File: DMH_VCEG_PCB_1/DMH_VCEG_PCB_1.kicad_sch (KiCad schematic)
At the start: 0 parts

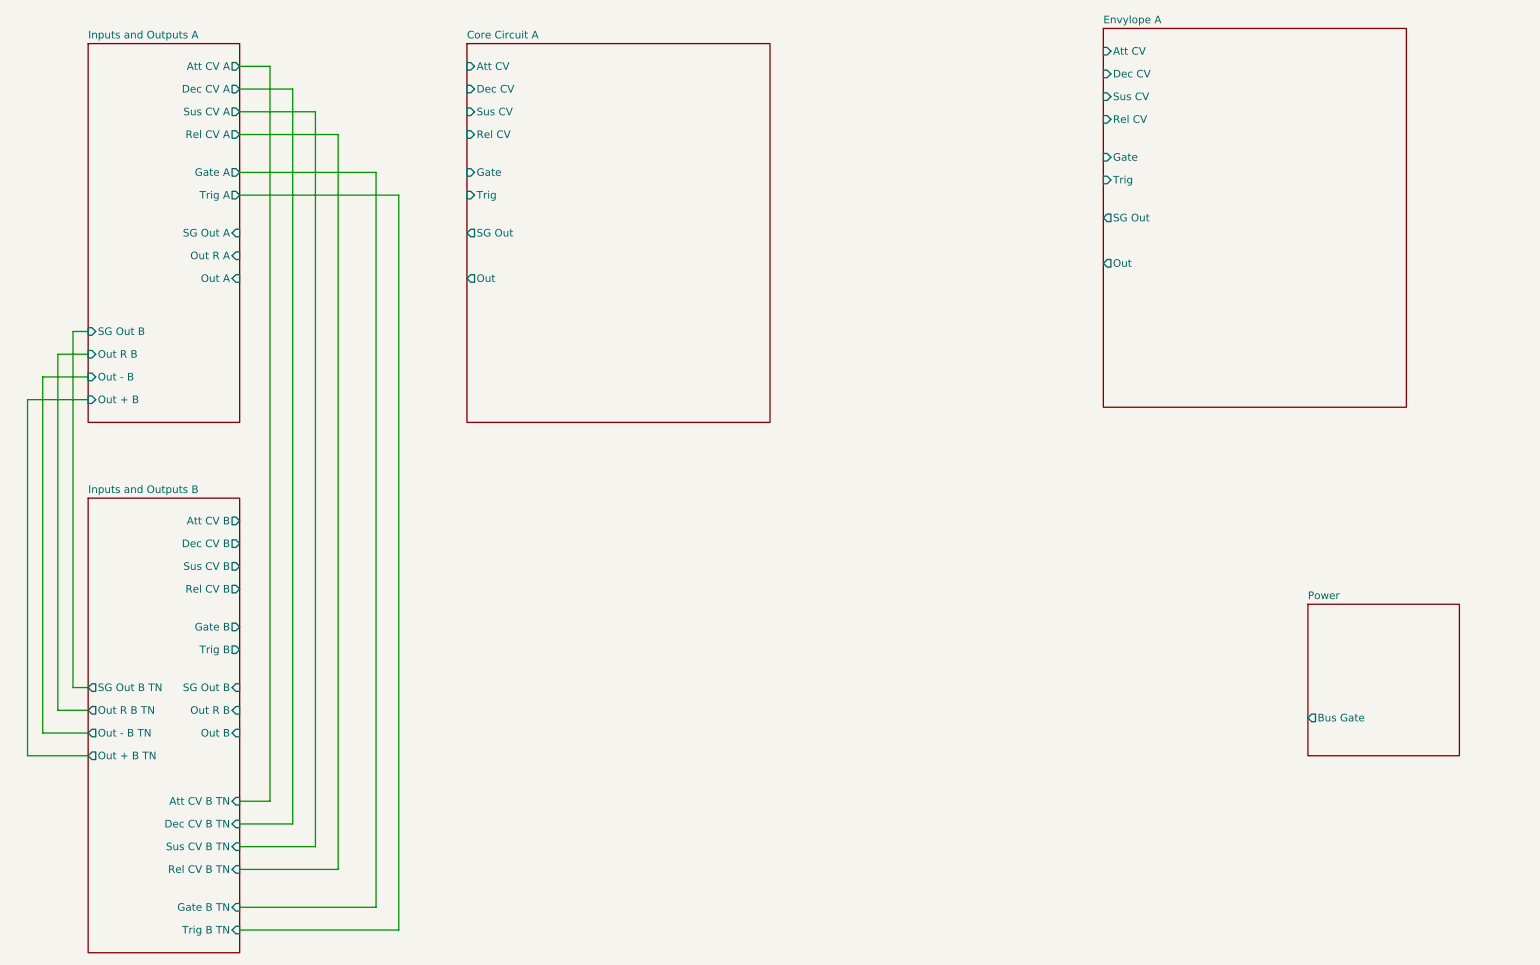
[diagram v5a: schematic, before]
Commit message: Implemented SG Out A
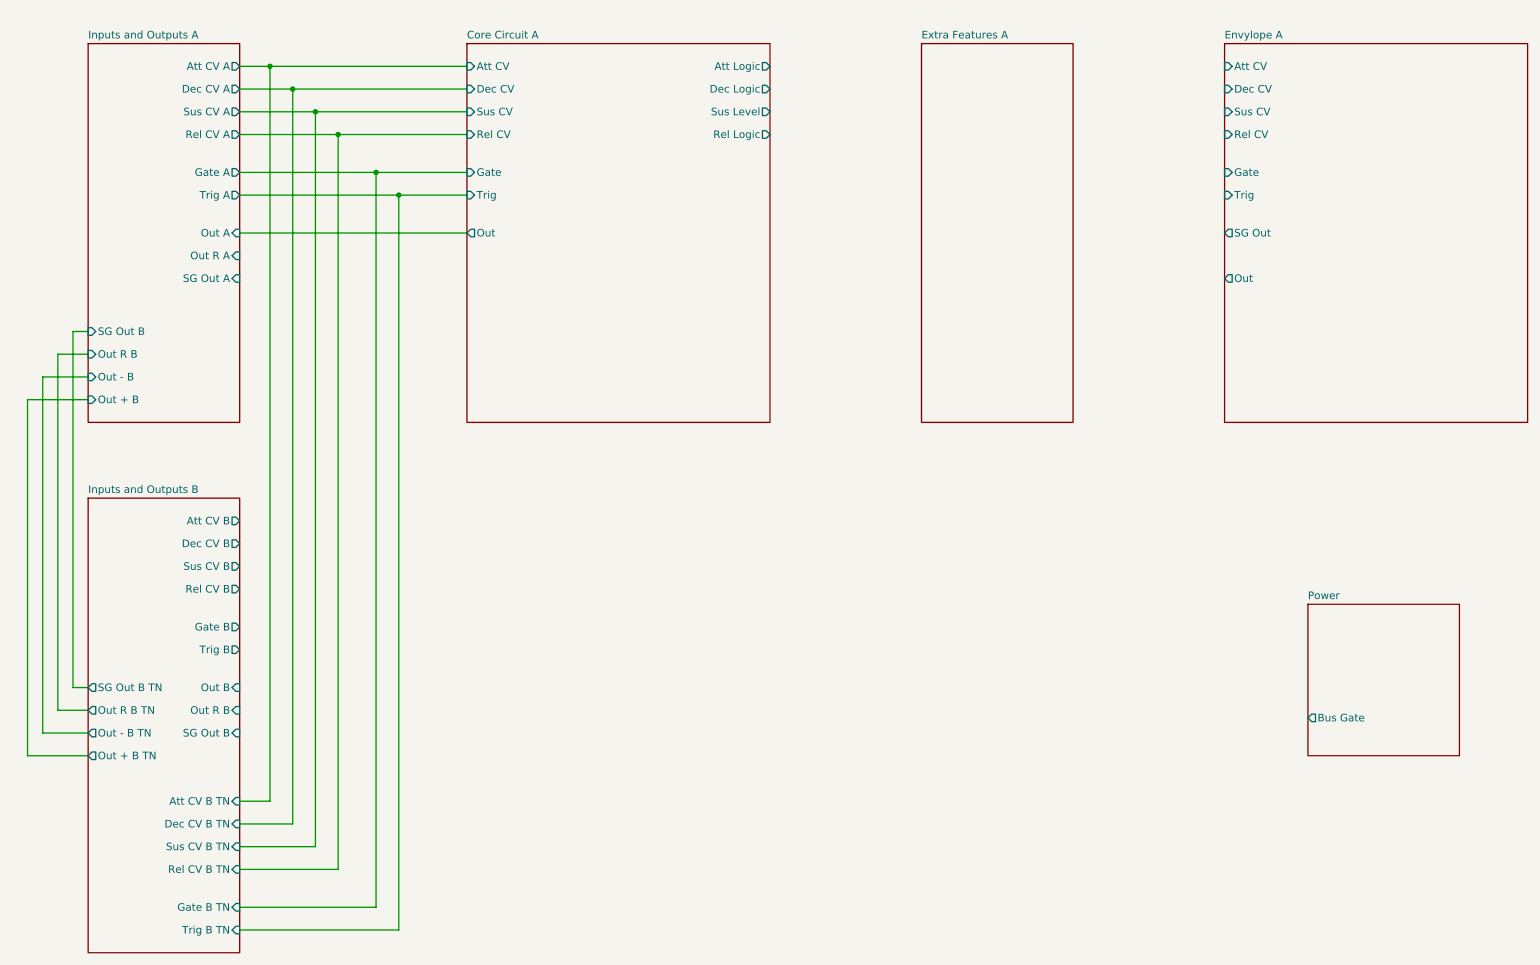
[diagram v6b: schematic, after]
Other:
- added sheet Extra Features A (Extra_Features_A.kicad_sch)
- sheet Core Circuit A ports: added Att Logic, Dec Logic, Rel Logic, Sus Level; removed SG Out
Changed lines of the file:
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@@
 		(comment 1 "PCB for 15cm Kosmo format synthesizer module")
 	)
+	(junction
+		(at 68.58 41.91)
+		(diameter 0)
+		(color 0 0 0 0)
+	)
+	(junction
+		(at 76.2 49.53)
+		(diameter 0)
+		(color 0 0 0 0)
+	)
+	(junction
+		(at 80.01 53.34)
+		(diameter 0)
+		(color 0 0 0 0)
+	)
+	(junction
+		(at 72.39 45.72)
+		(diameter 0)
+		(color 0 0 0 0)
+	)
+	(junction
+		(at 86.36 59.69)
+		(diameter 0)
+		(color 0 0 0 0)
+	)
+	(junction
+		(at 90.17 63.5)
+		(diameter 0)
+		(color 0 0 0 0)
+	)
 	(wire
 		(pts
@@
 	(wire
 		(pts
+			(xy 63.5 69.85) (xy 101.6 69.85)
+		)
+		(stroke
+			(width 0)
+			(type default)
+		)
+	)
+	(wire
+		(pts
 			(xy 63.5 172.72) (xy 76.2 172.72)
 		)
@@
 	(wire
 		(pts
+			(xy 86.36 59.69) (xy 101.6 59.69)
+		)
+		(stroke
+			(width 0)
+			(type default)
+		)
+	)
+	(wire
+		(pts
+			(xy 80.01 53.34) (xy 101.6 53.34)
+		)
+		(stroke
+			(width 0)
+			(type default)
+		)
+	)
+	(wire
+		(pts
 			(xy 63.5 186.69) (xy 90.17 186.69)
 		)
@@
 	(wire
 		(pts
+			(xy 76.2 49.53) (xy 101.6 49.53)
+		)
+		(stroke
+			(width 0)
+			(type default)
+		)
+	)
+	(wire
+		(pts
 			(xy 63.5 165.1) (xy 68.58 165.1)
 		)
@@
 	(wire
 		(pts
+			(xy 72.39 45.72) (xy 101.6 45.72)
+		)
+		(stroke
+			(width 0)
+			(type default)
+		)
+	)
+	(wire
+		(pts
 			(xy 63.5 168.91) (xy 72.39 168.91)
 		)
@@
 		(pts
 			(xy 30.48 153.67) (xy 30.48 93.98)
+		)
+		(stroke
+			(width 0)
+			(type default)
+		)
+	)
+	(wire
+		(pts
+			(xy 90.17 63.5) (xy 101.6 63.5)
+		)
+		(stroke
+			(width 0)
+			(type default)
+		)
+	)
+	(wire
+		(pts
+			(xy 68.58 41.91) (xy 101.6 41.91)
 		)
 		(stroke
@@
 		)
 		(pin "Out B" input
-			(at 63.5 153.67 0)
+			(at 63.5 146.05 0)
 			(effects
 				(font
@@
 		)
 		(pin "SG Out B" input
-			(at 63.5 146.05 0)
+			(at 63.5 153.67 0)
 			(effects
 				(font
@@
 	)
 	(sheet
-		(at 208.28 35.56)
+		(at 228.6 38.1)
 		(size 50.8 63.5)
 		(exclude_from_sim no)
@@
 		)
 		(property "Sheetname" "Envylope A"
-			(at 208.28 34.8484 0)
+			(at 228.6 37.3884 0)
 			(effects
 				(font
@@
 		)
 		(property "Sheetfile" "Envylope_A.kicad_sch"
-			(at 208.28 99.6446 0)
+			(at 228.6 102.1846 0)
 			(effects
 				(font
@@
 		)
 		(pin "Att CV" input
-			(at 208.28 39.37 180)
+			(at 228.6 41.91 180)
 			(effects
 				(font
@@
 		)
 		(pin "Dec CV" input
-			(at 208.28 43.18 180)
+			(at 228.6 45.72 180)
 			(effects
 				(font
@@
 		)
 		(pin "Gate" input
-			(at 208.28 57.15 180)
+			(at 228.6 59.69 180)
 			(effects
 				(font
@@
 		)
 		(pin "Rel CV" input
-			(at 208.28 50.8 180)
+			(at 228.6 53.34 180)
 			(effects
 				(font
@@
 		)
 		(pin "SG Out" output
-			(at 208.28 67.31 180)
+			(at 228.6 69.85 180)
 			(effects
 				(font
@@
 		)
 		(pin "Sus CV" input
-			(at 208.28 46.99 180)
+			(at 228.6 49.53 180)
 			(effects
 				(font
@@
 		)
 		(pin "Trig" input
-			(at 208.28 60.96 180)
+			(at 228.6 63.5 180)
 			(effects
 				(font
@@
 		)
 		(pin "Out" output
-			(at 208.28 74.93 180)
+			(at 228.6 77.47 180)
 			(effects
 				(font
@@
 			)
 		)
-		(pin "SG Out" output
-			(at 101.6 69.85 180)
-			(effects
-				(font
-					(size 1.27 1.27)
-				)
-				(justify left)
-			)
-		)
 		(pin "Sus CV" input
 			(at 101.6 49.53 180)
@@
 		)
 		(pin "Out" output
-			(at 101.6 77.47 180)
-			(effects
-				(font
-					(size 1.27 1.27)
-				)
-				(justify left)
+			(at 101.6 69.85 180)
+			(effects
+				(font
+					(size 1.27 1.27)
+				)
+				(justify left)
+			)
+		)
+		(pin "Att Logic" output
+			(at 152.4 41.91 0)
+			(effects
+				(font
+					(size 1.27 1.27)
+				)
+				(justify right)
+			)
+		)
+		(pin "Dec Logic" output
+			(at 152.4 45.72 0)
+			(effects
+				(font
+					(size 1.27 1.27)
+				)
+				(justify right)
+			)
+		)
+		(pin "Rel Logic" output
+			(at 152.4 53.34 0)
+			(effects
+				(font
+					(size 1.27 1.27)
+				)
+				(justify right)
+			)
+		)
+		(pin "Sus Level" output
+			(at 152.4 49.53 0)
+			(effects
+				(font
+					(size 1.27 1.27)
+				)
+				(justify right)
 			)
 		)
@@
 		)
 		(pin "Out A" input
-			(at 63.5 77.47 0)
+			(at 63.5 69.85 0)
 			(effects
 				(font
@@
 		)
 		(pin "SG Out A" input
-			(at 63.5 69.85 0)
+			(at 63.5 77.47 0)
 			(effects
 				(font
@@
 				)
 			)
+		)
+	)
+	(sheet
+		(at 177.8 38.1)
+		(size 25.4 63.5)
+		(exclude_from_sim no)
+		(in_bom yes)
+		(on_board yes)
+		(dnp no)
+		(fields_autoplaced yes)
+		(stroke
+			(width 0.1524)
+			(type solid)
+		)
+		(fill
+			(color 0 0 0 0.0000)
+		)
+		(property "Sheetname" "Extra Features A"
+			(at 177.8 37.3884 0)
+			(effects
+				(font
+					(size 1.27 1.27)
+				)
+				(justify left bottom)
+			)
+		)
+		(property "Sheetfile" "Extra_Features_A.kicad_sch"
+			(at 177.8 102.1846 0)
+			(effects
+				(font
+					(size 1.27 1.27)
+				)
+				(justify left top)
+				(hide yes)
+			)
+		)
+		(instances
+			(project "DMH_VCEG_PCB_1"
+				(path "/58f4306d-5387-4983-bb08-41a2313fd315"
+					(page "7")
+				)
+			)

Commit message: Added Out R
Ready for breadboarding
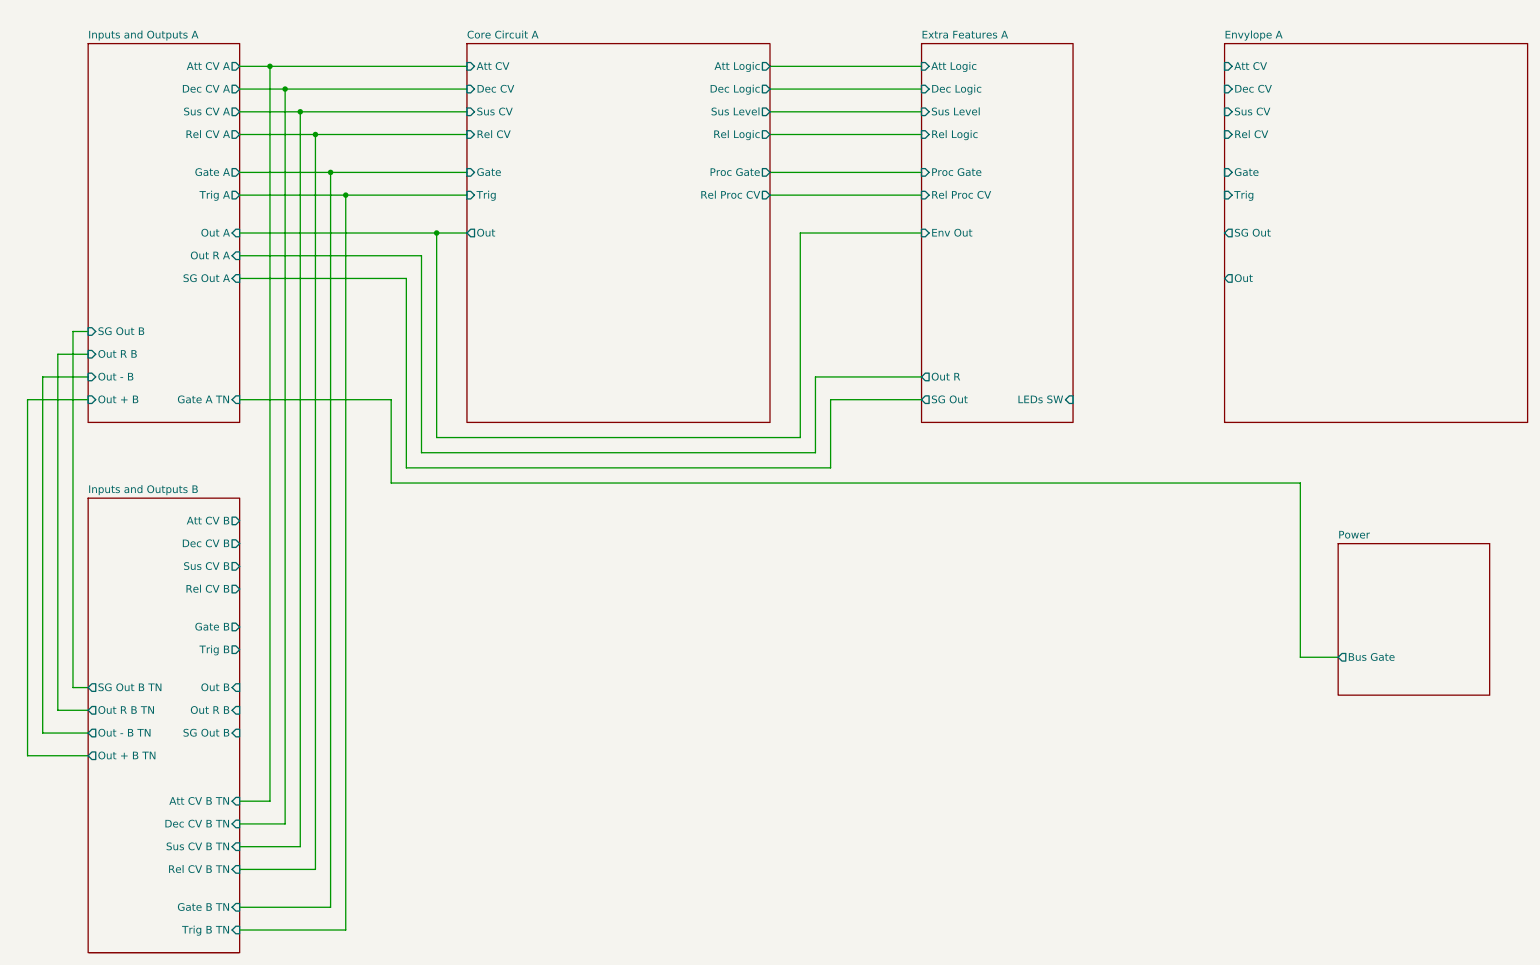
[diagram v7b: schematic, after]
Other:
- sheet Core Circuit A ports: added Proc Gate, Rel Proc CV; removed none
- sheet Extra Features A ports: added Att Logic, Dec Logic, Env Out, LEDs SW, Out R, Proc Gate, Rel Logic, Rel Proc CV, SG Out, Sus Level; removed none
- sheet Inputs and Outputs A ports: added Gate A TN; removed none

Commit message: Corrected Out R design
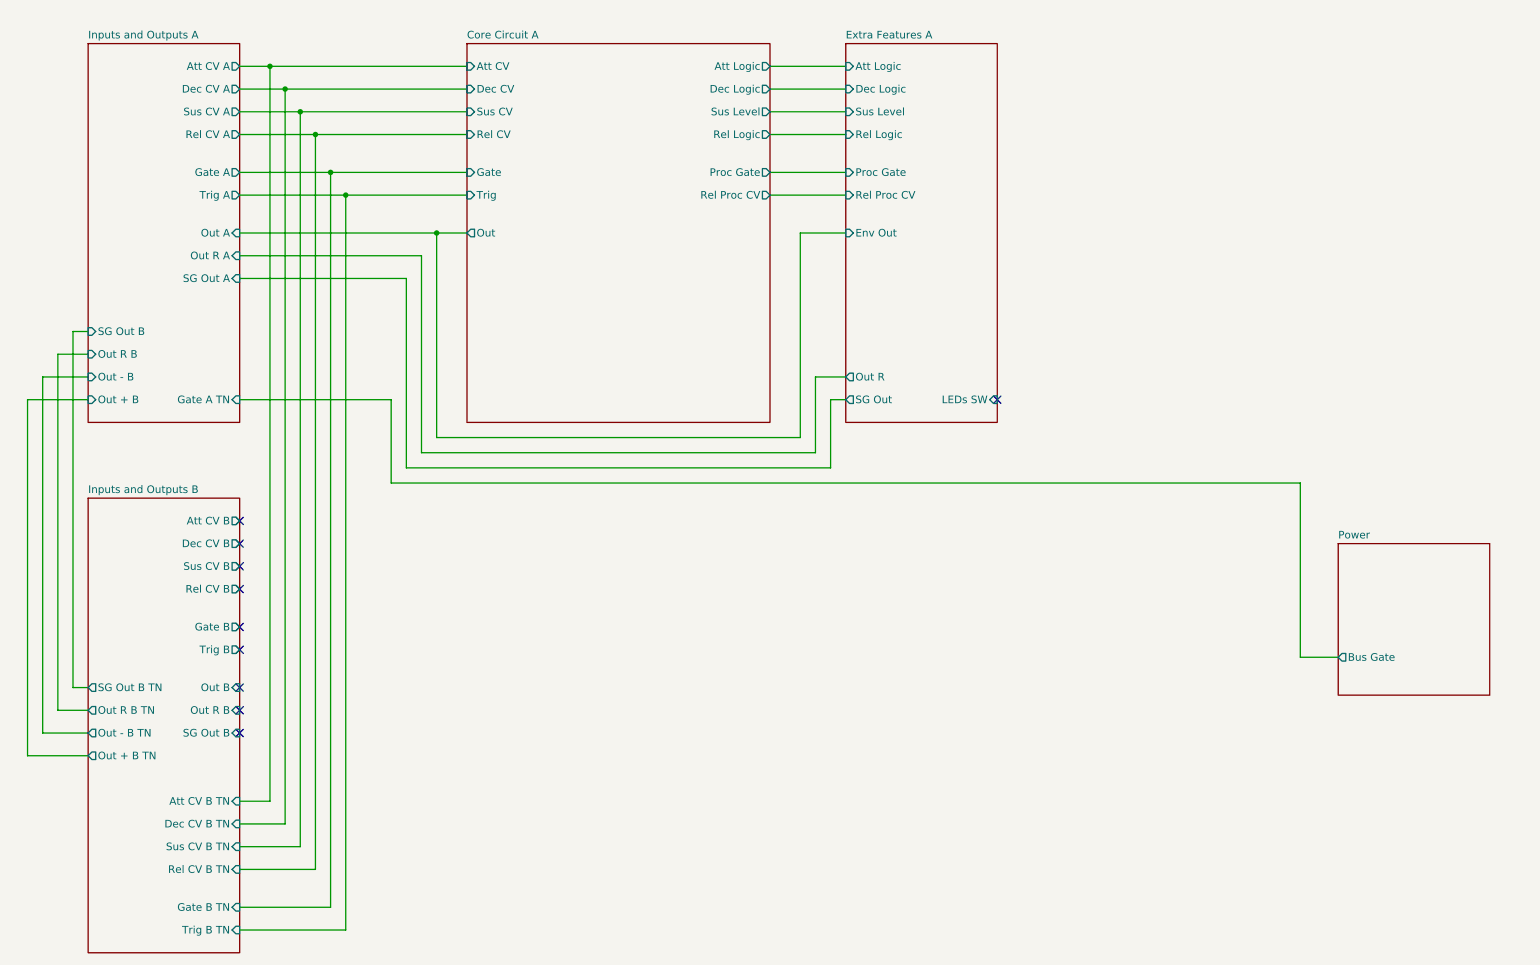
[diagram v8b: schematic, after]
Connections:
- no-connect marks 0 -> 10
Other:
- removed sheet Envylope A
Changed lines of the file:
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@@
 		(color 0 0 0 0)
 	)
-	(wire
-		(pts
-			(xy 152.4 41.91) (xy 177.8 41.91)
+	(no_connect
+		(at 190.5 97.79)
+	)
+	(no_connect
+		(at 63.5 146.05)
+	)
+	(no_connect
+		(at 63.5 149.86)
+	)
+	(no_connect
+		(at 63.5 125.73)
+	)
+	(no_connect
+		(at 63.5 118.11)
+	)
+	(no_connect
+		(at 63.5 121.92)
+	)
+	(no_connect
+		(at 63.5 139.7)
+	)
+	(no_connect
+		(at 63.5 153.67)
+	)
+	(no_connect
+		(at 63.5 135.89)
+	)
+	(no_connect
+		(at 63.5 129.54)
+	)
+	(wire
+		(pts
+			(xy 152.4 41.91) (xy 165.1 41.91)
 		)
 		(stroke
@@
 	(wire
 		(pts
-			(xy 177.8 93.98) (xy 160.02 93.98)
+			(xy 165.1 93.98) (xy 160.02 93.98)
 		)
 		(stroke
@@
 	(wire
 		(pts
-			(xy 157.48 69.85) (xy 177.8 69.85)
+			(xy 157.48 69.85) (xy 165.1 69.85)
 		)
 		(stroke
@@
 	(wire
 		(pts
-			(xy 152.4 45.72) (xy 177.8 45.72)
+			(xy 152.4 45.72) (xy 165.1 45.72)
 		)
 		(stroke
@@
 	(wire
 		(pts
-			(xy 152.4 63.5) (xy 177.8 63.5)
+			(xy 152.4 63.5) (xy 165.1 63.5)
 		)
 		(stroke
@@
 	(wire
 		(pts
-			(xy 152.4 49.53) (xy 177.8 49.53)
-		)
-		(stroke
-			(width 0)
-			(type default)
-		)
-	)
-	(wire
-		(pts
-			(xy 152.4 53.34) (xy 177.8 53.34)
+			(xy 152.4 49.53) (xy 165.1 49.53)
+		)
+		(stroke
+			(width 0)
+			(type default)
+		)
+	)
+	(wire
+		(pts
+			(xy 152.4 53.34) (xy 165.1 53.34)
 		)
 		(stroke
@@
 	(wire
 		(pts
-			(xy 152.4 59.69) (xy 177.8 59.69)
+			(xy 152.4 59.69) (xy 165.1 59.69)
 		)
 		(stroke
@@
 	(wire
 		(pts
-			(xy 162.56 97.79) (xy 177.8 97.79)
+			(xy 162.56 97.79) (xy 165.1 97.79)
 		)
 		(stroke
@@
 			(project "DMH_VCEG_PCB_1"
 				(path "/58f4306d-5387-4983-bb08-41a2313fd315"
-					(page "4")
+					(page "10")
 				)
 			)
@@
 	)
 	(sheet
-		(at 228.6 38.1)
-		(size 50.8 63.5)
-		(exclude_from_sim no)
-		(in_bom yes)
-		(on_board yes)
-		(dnp no)
-		(fields_autoplaced yes)
-		(stroke
-			(width 0.1524)
-			(type solid)
-		)
-		(fill
-			(color 0 0 0 0.0000)
-		)
-		(property "Sheetname" "Envylope A"
-			(at 228.6 37.3884 0)
-			(effects
-				(font
-					(size 1.27 1.27)
-				)
-				(justify left bottom)
-			)
-		)
-		(property "Sheetfile" "Envylope_A.kicad_sch"
-			(at 228.6 102.1846 0)
-			(effects
-				(font
-					(size 1.27 1.27)
-				)
-				(justify left top)
-				(hide yes)
-			)
-		)
-		(pin "Att CV" input
-			(at 228.6 41.91 180)
-			(effects
-				(font
-					(size 1.27 1.27)
-				)
-				(justify left)
-			)
-		)
-		(pin "Dec CV" input
-			(at 228.6 45.72 180)
-			(effects
-				(font
-					(size 1.27 1.27)
-				)
-				(justify left)
-			)
-		)
-		(pin "Gate" input
-			(at 228.6 59.69 180)
-			(effects
-				(font
-					(size 1.27 1.27)
-				)
-				(justify left)
-			)
-		)
-		(pin "Rel CV" input
-			(at 228.6 53.34 180)
-			(effects
-				(font
-					(size 1.27 1.27)
-				)
-				(justify left)
-			)
-		)
-		(pin "SG Out" output
-			(at 228.6 69.85 180)
-			(effects
-				(font
-					(size 1.27 1.27)
-				)
-				(justify left)
-			)
-		)
-		(pin "Sus CV" input
-			(at 228.6 49.53 180)
-			(effects
-				(font
-					(size 1.27 1.27)
-				)
-				(justify left)
-			)
-		)
-		(pin "Trig" input
-			(at 228.6 63.5 180)
-			(effects
-				(font
-					(size 1.27 1.27)
-				)
-				(justify left)
-			)
-		)
-		(pin "Out" output
-			(at 228.6 77.47 180)
-			(effects
-				(font
-					(size 1.27 1.27)
-				)
-				(justify left)
-			)
-		)
-		(instances
-			(project "DMH_VCEG_PCB_1"
-				(path "/58f4306d-5387-4983-bb08-41a2313fd315"
-					(page "4")
-				)
-			)
-		)
-	)
-	(sheet
 		(at 101.6 38.1)
 		(size 50.8 63.5)
@@
 	)
 	(sheet
-		(at 177.8 38.1)
+		(at 165.1 38.1)
 		(size 25.4 63.5)
 		(exclude_from_sim no)
@@
 		)
 		(property "Sheetname" "Extra Features A"
-			(at 177.8 37.3884 0)
+			(at 165.1 37.3884 0)
 			(effects
 				(font
@@
 		)
 		(property "Sheetfile" "Extra_Features_A.kicad_sch"
-			(at 177.8 102.1846 0)
+			(at 165.1 102.1846 0)
 			(effects
 				(font
@@
 		)
 		(pin "Att Logic" input
-			(at 177.8 41.91 180)
+			(at 165.1 41.91 180)
 			(effects
 				(font
@@
 		)
 		(pin "Dec Logic" input
-			(at 177.8 45.72 180)
+			(at 165.1 45.72 180)
 			(effects
 				(font
@@
 		)
 		(pin "Env Out" input
-			(at 177.8 69.85 180)
+			(at 165.1 69.85 180)
 			(effects
 				(font
@@
 		)
 		(pin "Out R" output
-			(at 177.8 93.98 180)
+			(at 165.1 93.98 180)
 			(effects
 				(font
@@
 		)
 		(pin "Proc Gate" input
-			(at 177.8 59.69 180)
+			(at 165.1 59.69 180)
 			(effects
 				(font
@@
 		)
 		(pin "Rel Logic" input
-			(at 177.8 53.34 180)
+			(at 165.1 53.34 180)
 			(effects
 				(font
@@
 		)
 		(pin "Rel Proc CV" input
-			(at 177.8 63.5 180)
+			(at 165.1 63.5 180)
 			(effects
 				(font
@@
 		)
 		(pin "SG Out" output
-			(at 177.8 97.79 180)
+			(at 165.1 97.79 180)
 			(effects
 				(font
@@
 		)
 		(pin "Sus Level" input
-			(at 177.8 49.53 180)
+			(at 165.1 49.53 180)
 			(effects
 				(font
@@
 		)
 		(pin "LEDs SW" input
-			(at 203.2 97.79 0)
-			(effects
-				(font
+			(at 190.5 97.79 0)
+			(effects
+				(font
